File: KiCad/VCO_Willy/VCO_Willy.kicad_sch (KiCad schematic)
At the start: 50 parts, among them J1 Conn_02x07_Odd_Even, J2 Conn_02x07_Odd_Even, J3 Conn_01x03_Male, J4 Conn_01x03_Male, J5 Conn_01x03_Male, U1 TL074, U2 TL074, U3 TL074

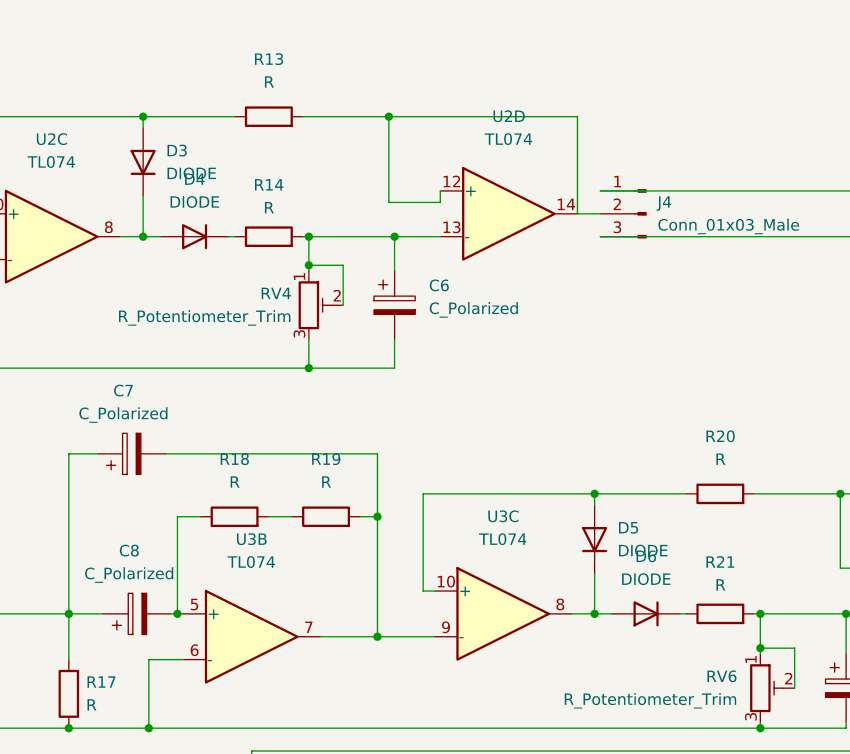
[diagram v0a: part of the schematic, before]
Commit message: Dämpfer,Filter,Peak implementiert auf PCB
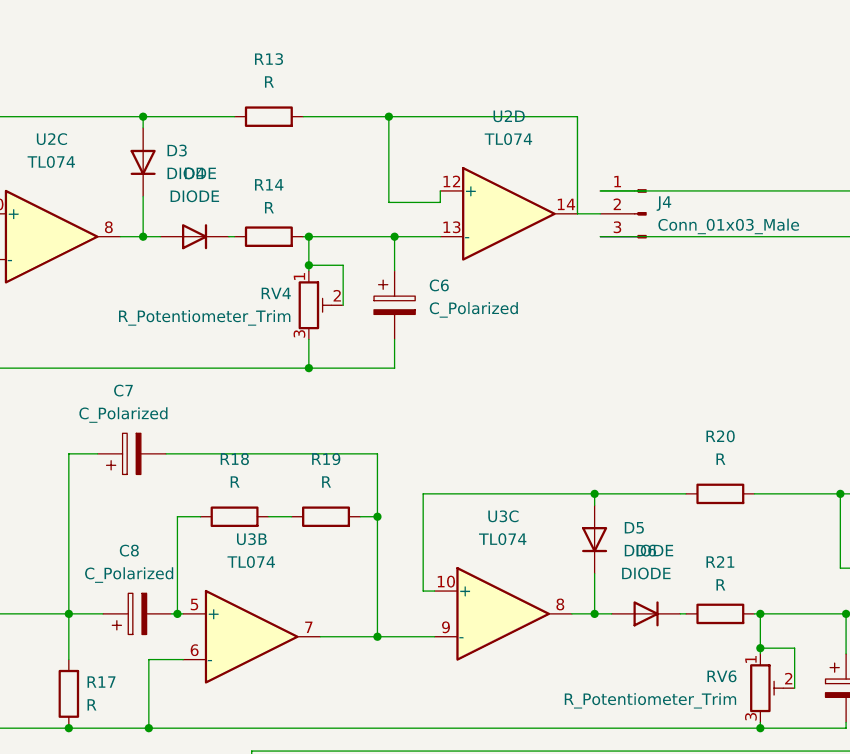
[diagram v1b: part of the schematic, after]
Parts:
- D1, D2, D3, D4, D5, D6: footprint Diode_THT:D_DO-201AE_P3.81mm_Vertical_KathodeUp -> Diode_THT:D_A-405_P10.16mm_Horizontal
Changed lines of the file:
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@@
   (symbol (lib_id "Simulation_SPICE:DIODE") (at 213.36 135.255 0) (unit 1)
     (in_bom yes) (on_board yes) (fields_autoplaced)
-    (property "Reference" "D6" (id 0) (at 213.36 128.905 0))
-    (property "Value" "DIODE" (id 1) (at 213.36 131.445 0))
-    (property "Footprint" "Diode_THT:D_DO-201AE_P3.81mm_Vertical_KathodeUp" (id 2) (at 213.36 135.255 0)
+    (property "Reference" "D6" (id 0) (at 213.36 128.27 0))
+    (property "Value" "DIODE" (id 1) (at 213.36 130.81 0))
+    (property "Footprint" "Diode_THT:D_A-405_P10.16mm_Horizontal" (id 2) (at 213.36 135.255 0)
       (effects (font (size 1.27 1.27)) hide)
     )
@@
       (effects (font (size 1.27 1.27)) (justify left))
     )
-    (property "Footprint" "Diode_THT:D_DO-201AE_P3.81mm_Vertical_KathodeUp" (id 2) (at 147.32 36.195 0)
+    (property "Footprint" "Diode_THT:D_A-405_P10.16mm_Horizontal" (id 2) (at 147.32 36.195 0)
       (effects (font (size 1.27 1.27)) hide)
     )
@@
     (property "Reference" "D2" (id 0) (at 153.035 38.1 0))
     (property "Value" "DIODE" (id 1) (at 153.035 40.64 0))
-    (property "Footprint" "Diode_THT:D_DO-201AE_P3.81mm_Vertical_KathodeUp" (id 2) (at 153.035 44.45 0)
+    (property "Footprint" "Diode_THT:D_A-405_P10.16mm_Horizontal" (id 2) (at 153.035 44.45 0)
       (effects (font (size 1.27 1.27)) hide)
     )
@@
   (symbol (lib_id "Simulation_SPICE:DIODE") (at 163.195 93.345 0) (unit 1)
     (in_bom yes) (on_board yes) (fields_autoplaced)
-    (property "Reference" "D4" (id 0) (at 163.195 86.995 0))
-    (property "Value" "DIODE" (id 1) (at 163.195 89.535 0))
-    (property "Footprint" "Diode_THT:D_DO-201AE_P3.81mm_Vertical_KathodeUp" (id 2) (at 163.195 93.345 0)
+    (property "Reference" "D4" (id 0) (at 163.195 86.36 0))
+    (property "Value" "DIODE" (id 1) (at 163.195 88.9 0))
+    (property "Footprint" "Diode_THT:D_A-405_P10.16mm_Horizontal" (id 2) (at 163.195 93.345 0)
       (effects (font (size 1.27 1.27)) hide)
     )
@@
       (effects (font (size 1.27 1.27)) (justify left))
     )
-    (property "Footprint" "Diode_THT:D_DO-201AE_P3.81mm_Vertical_KathodeUp" (id 2) (at 157.48 85.09 0)
+    (property "Footprint" "Diode_THT:D_A-405_P10.16mm_Horizontal" (id 2) (at 157.48 85.09 0)
       (effects (font (size 1.27 1.27)) hide)
     )
@@
   (symbol (lib_id "Simulation_SPICE:DIODE") (at 207.645 127 270) (unit 1)
     (in_bom yes) (on_board yes) (fields_autoplaced)
-    (property "Reference" "D5" (id 0) (at 210.185 125.7299 90)
-      (effects (font (size 1.27 1.27)) (justify left))
-    )
-    (property "Value" "DIODE" (id 1) (at 210.185 128.2699 90)
-      (effects (font (size 1.27 1.27)) (justify left))
-    )
-    (property "Footprint" "Diode_THT:D_DO-201AE_P3.81mm_Vertical_KathodeUp" (id 2) (at 207.645 127 0)
+    (property "Reference" "D5" (id 0) (at 210.82 125.7299 90)
+      (effects (font (size 1.27 1.27)) (justify left))
+    )
+    (property "Value" "DIODE" (id 1) (at 210.82 128.2699 90)
+      (effects (font (size 1.27 1.27)) (justify left))
+    )
+    (property "Footprint" "Diode_THT:D_A-405_P10.16mm_Horizontal" (id 2) (at 207.645 127 0)
       (effects (font (size 1.27 1.27)) hide)
     )
@@
     )
     (path "/63870de2-3288-4c04-9dca-6c24c271a28e"
-      (reference "D1") (unit 1) (value "DIODE") (footprint "Diode_THT:D_DO-201AE_P3.81mm_Vertical_KathodeUp")
+      (reference "D1") (unit 1) (value "DIODE") (footprint "Diode_THT:D_A-405_P10.16mm_Horizontal")
     )
     (path "/6d6a438a-2292-412e-a826-736e36cd916a"
-      (reference "D2") (unit 1) (value "DIODE") (footprint "Diode_THT:D_DO-201AE_P3.81mm_Vertical_KathodeUp")
+      (reference "D2") (unit 1) (value "DIODE") (footprint "Diode_THT:D_A-405_P10.16mm_Horizontal")
     )
     (path "/adaf29f7-8f73-4f45-adc0-cce76f7a31ae"
-      (reference "D3") (unit 1) (value "DIODE") (footprint "Diode_THT:D_DO-201AE_P3.81mm_Vertical_KathodeUp")
+      (reference "D3") (unit 1) (value "DIODE") (footprint "Diode_THT:D_A-405_P10.16mm_Horizontal")
     )
     (path "/760d2d48-b66b-4427-b8bb-9fe043aa67f7"
-      (reference "D4") (unit 1) (value "DIODE") (footprint "Diode_THT:D_DO-201AE_P3.81mm_Vertical_KathodeUp")
+      (reference "D4") (unit 1) (value "DIODE") (footprint "Diode_THT:D_A-405_P10.16mm_Horizontal")
     )
     (path "/b86c2930-1e38-4fd9-8c93-0b7d1f9f6f0c"
-      (reference "D5") (unit 1) (value "DIODE") (footprint "Diode_THT:D_DO-201AE_P3.81mm_Vertical_KathodeUp")
+      (reference "D5") (unit 1) (value "DIODE") (footprint "Diode_THT:D_A-405_P10.16mm_Horizontal")
     )
     (path "/39bcfd97-ac80-4e29-a89e-0996dfb6adc1"
-      (reference "D6") (unit 1) (value "DIODE") (footprint "Diode_THT:D_DO-201AE_P3.81mm_Vertical_KathodeUp")
+      (reference "D6") (unit 1) (value "DIODE") (footprint "Diode_THT:D_A-405_P10.16mm_Horizontal")
     )
     (path "/787ffbaa-27cf-4b37-81cb-8916032c1a87"

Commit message: upload new design
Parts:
- D1, D2, D3, D4, D5, D6: footprint Diode_THT:D_A-405_P10.16mm_Horizontal -> Diode_THT:D_DO-35_SOD27_P7.62mm_Horizontal
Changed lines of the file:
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@@
     (property "Reference" "D6" (id 0) (at 213.36 128.27 0))
     (property "Value" "DIODE" (id 1) (at 213.36 130.81 0))
-    (property "Footprint" "Diode_THT:D_A-405_P10.16mm_Horizontal" (id 2) (at 213.36 135.255 0)
+    (property "Footprint" "Diode_THT:D_DO-35_SOD27_P7.62mm_Horizontal" (id 2) (at 213.36 135.255 0)
       (effects (font (size 1.27 1.27)) hide)
     )
@@
       (effects (font (size 1.27 1.27)) (justify left))
     )
-    (property "Footprint" "Diode_THT:D_A-405_P10.16mm_Horizontal" (id 2) (at 147.32 36.195 0)
+    (property "Footprint" "Diode_THT:D_DO-35_SOD27_P7.62mm_Horizontal" (id 2) (at 147.32 36.195 0)
       (effects (font (size 1.27 1.27)) hide)
     )
@@
     (property "Reference" "D2" (id 0) (at 153.035 38.1 0))
     (property "Value" "DIODE" (id 1) (at 153.035 40.64 0))
-    (property "Footprint" "Diode_THT:D_A-405_P10.16mm_Horizontal" (id 2) (at 153.035 44.45 0)
+    (property "Footprint" "Diode_THT:D_DO-35_SOD27_P7.62mm_Horizontal" (id 2) (at 153.035 44.45 0)
       (effects (font (size 1.27 1.27)) hide)
     )
@@
     (property "Reference" "D4" (id 0) (at 163.195 86.36 0))
     (property "Value" "DIODE" (id 1) (at 163.195 88.9 0))
-    (property "Footprint" "Diode_THT:D_A-405_P10.16mm_Horizontal" (id 2) (at 163.195 93.345 0)
+    (property "Footprint" "Diode_THT:D_DO-35_SOD27_P7.62mm_Horizontal" (id 2) (at 163.195 93.345 0)
       (effects (font (size 1.27 1.27)) hide)
     )
@@
       (effects (font (size 1.27 1.27)) (justify left))
     )
-    (property "Footprint" "Diode_THT:D_A-405_P10.16mm_Horizontal" (id 2) (at 157.48 85.09 0)
+    (property "Footprint" "Diode_THT:D_DO-35_SOD27_P7.62mm_Horizontal" (id 2) (at 157.48 85.09 0)
       (effects (font (size 1.27 1.27)) hide)
     )
@@
       (effects (font (size 1.27 1.27)) (justify left))
     )
-    (property "Footprint" "Diode_THT:D_A-405_P10.16mm_Horizontal" (id 2) (at 207.645 127 0)
+    (property "Footprint" "Diode_THT:D_DO-35_SOD27_P7.62mm_Horizontal" (id 2) (at 207.645 127 0)
       (effects (font (size 1.27 1.27)) hide)
     )
@@
     )
     (path "/63870de2-3288-4c04-9dca-6c24c271a28e"
-      (reference "D1") (unit 1) (value "DIODE") (footprint "Diode_THT:D_A-405_P10.16mm_Horizontal")
+      (reference "D1") (unit 1) (value "DIODE") (footprint "Diode_THT:D_DO-35_SOD27_P7.62mm_Horizontal")
     )
     (path "/6d6a438a-2292-412e-a826-736e36cd916a"
-      (reference "D2") (unit 1) (value "DIODE") (footprint "Diode_THT:D_A-405_P10.16mm_Horizontal")
+      (reference "D2") (unit 1) (value "DIODE") (footprint "Diode_THT:D_DO-35_SOD27_P7.62mm_Horizontal")
     )
     (path "/adaf29f7-8f73-4f45-adc0-cce76f7a31ae"
-      (reference "D3") (unit 1) (value "DIODE") (footprint "Diode_THT:D_A-405_P10.16mm_Horizontal")
+      (reference "D3") (unit 1) (value "DIODE") (footprint "Diode_THT:D_DO-35_SOD27_P7.62mm_Horizontal")
     )
     (path "/760d2d48-b66b-4427-b8bb-9fe043aa67f7"
-      (reference "D4") (unit 1) (value "DIODE") (footprint "Diode_THT:D_A-405_P10.16mm_Horizontal")
+      (reference "D4") (unit 1) (value "DIODE") (footprint "Diode_THT:D_DO-35_SOD27_P7.62mm_Horizontal")
     )
     (path "/b86c2930-1e38-4fd9-8c93-0b7d1f9f6f0c"
-      (reference "D5") (unit 1) (value "DIODE") (footprint "Diode_THT:D_A-405_P10.16mm_Horizontal")
+      (reference "D5") (unit 1) (value "DIODE") (footprint "Diode_THT:D_DO-35_SOD27_P7.62mm_Horizontal")
     )
     (path "/39bcfd97-ac80-4e29-a89e-0996dfb6adc1"
-      (reference "D6") (unit 1) (value "DIODE") (footprint "Diode_THT:D_A-405_P10.16mm_Horizontal")
+      (reference "D6") (unit 1) (value "DIODE") (footprint "Diode_THT:D_DO-35_SOD27_P7.62mm_Horizontal")
     )
     (path "/787ffbaa-27cf-4b37-81cb-8916032c1a87"
